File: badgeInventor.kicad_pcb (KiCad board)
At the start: 2 copper layers, 89.2 x 86 mm, 35 parts, among them P1 AUTO-PROGRAM JUMPER, P2 CONN_01X10, P22 CONN_01X10, P23 CONN_01X10, P3 LiPo, P5 OLED_I2C, P6 USB Serial, SW1 RESET, U1 SPX1117, U2 MCP73831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

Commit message: PCB v0.01
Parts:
- added SW2: SW_PUSH, open-project:SW_PUSH_SMD, F.Cu at (124.5, 146.3)
- P3: moved to B.Cu
- moved C1 59.5 mm to (115.8, 148.2), turned to 180 degrees
- moved P3 40.7 mm to (141.2, 113.5), turned to 180 degrees
- moved D5 38.7 mm to (122.7, 108.0), turned to 90 degrees
- moved D2 36.4 mm to (127.8, 108.0), turned to 270 degrees
- moved R9 30.7 mm to (149.1, 119.4)
- moved R1 29.2 mm to (164.1, 148.1), turned to 180 degrees
- moved R11 29.1 mm to (137.8, 123.4), turned to 270 degrees
- moved C5 25.0 mm to (143.3, 108.0), turned to 90 degrees
- moved D4 20.8 mm to (122.7, 137.9), turned to 90 degrees
- moved P6 20.1 mm to (132.3, 101.3)
- moved U2 20.0 mm to (149.6, 112.3)
- moved P1 18.8 mm to (119.1, 118.4), turned to 270 degrees
- moved R4 18.6 mm to (148.6, 106.9), turned to 270 degrees
- moved R10 17.7 mm to (126.2, 136.4)
- moved R3 15.4 mm to (124.7, 129.0), turned to 90 degrees
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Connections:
- P22 pad 2: /ESP8266/GPIO0 -> GND
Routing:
- net +3V3: track 1.24 -> 142.5 mm, vias 0 -> 2
- net GND: track 12.6 -> 115.2 mm, vias 0 -> 2
- net +BATT: track 0.00 -> 98.6 mm, vias 0 -> 2
- net /ESP8266/RX: track 0.00 -> 77.6 mm
- net VCC: track 11.3 -> 80.6 mm
- net /ESP8266/DTR: track 0.00 -> 61.9 mm
- net /ESP8266/GPIO14: track 0.00 -> 60.3 mm, vias 0 -> 1
- net /ESP8266/CH_PD: track 0.00 -> 59.9 mm, vias 0 -> 2
- net /ESP8266/TX: track 0.05 -> 57.7 mm, vias 0 -> 1
- net /ESP8266/RST: track 0.66 -> 49.4 mm, vias 0 -> 2
- net /ESP8266/GPIO0: track 0.12 -> 35.4 mm
- net /ESP8266/GPIO12: track 0.00 -> 31.5 mm, vias 0 -> 1
- net /ESP8266/GPIO15: track 0.00 -> 28.9 mm, vias 0 -> 1
- net /ESP8266/GPIO2: track 0.23 -> 28.3 mm
- net /ESP8266/GPIO4/SDA: track 18.3 -> 41.3 mm, vias 0 -> 1
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- added copper zone on B.Cu, net GND
- added copper zone on F.Cu, net GND
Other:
- board outline removed
- net class Vcc added: clearance 0.2, trace_width 0.31, via_dia 0.6, via_drill 0.4

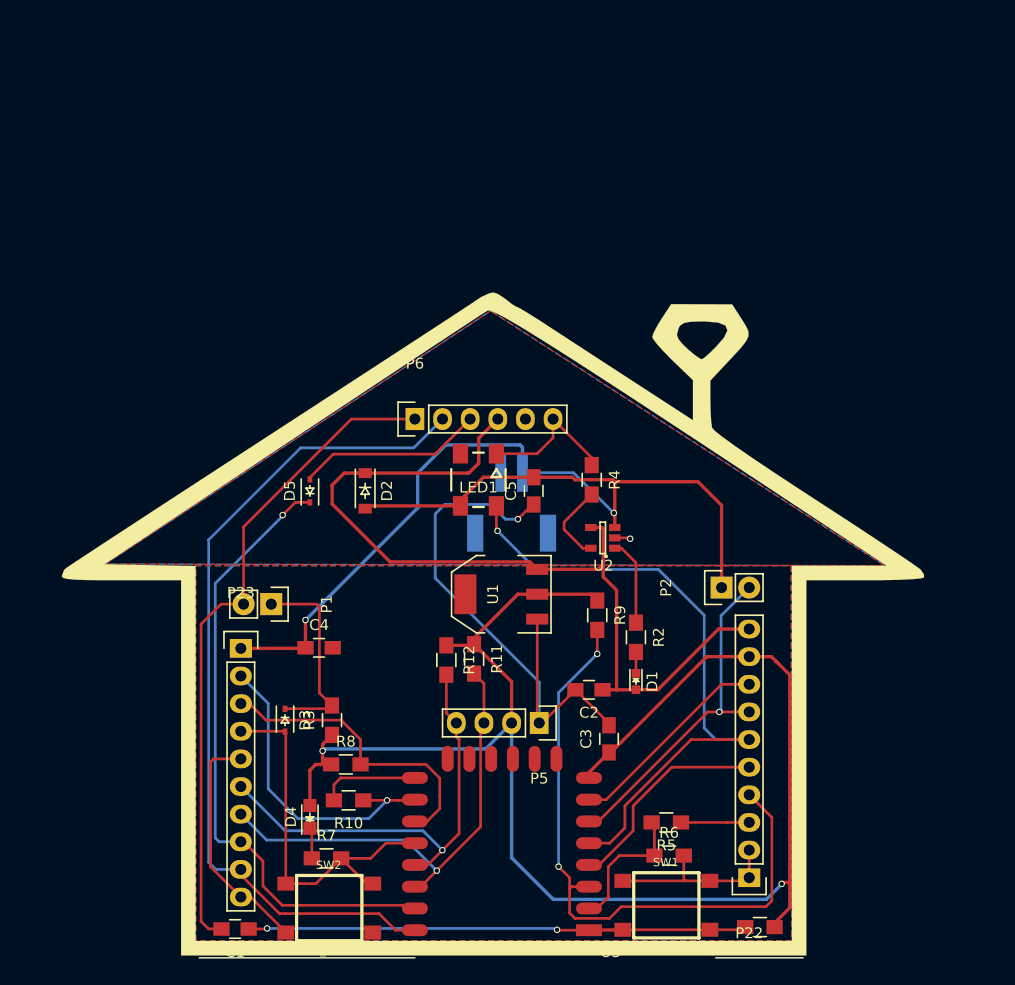
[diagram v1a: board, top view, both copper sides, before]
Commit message: Agregado EdgeCut, reacomodo de etiquetas y nombre de Serial
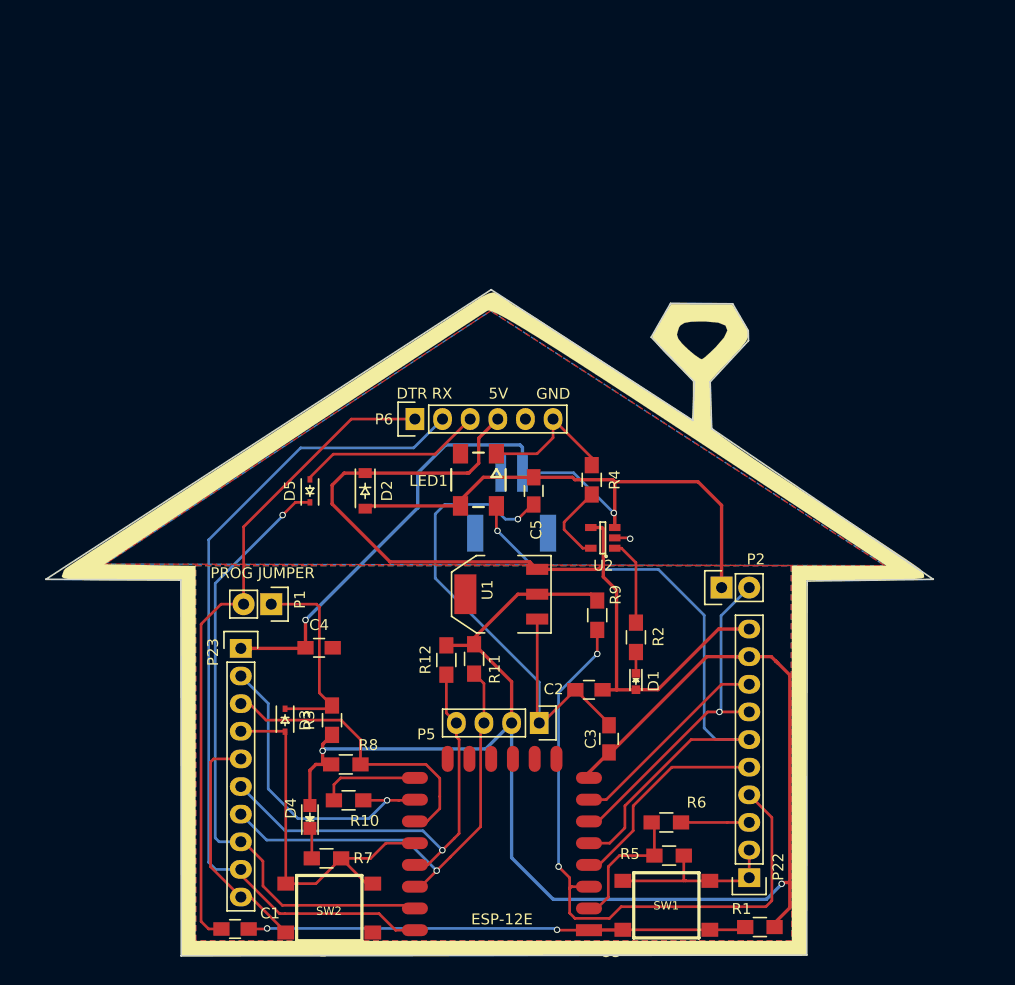
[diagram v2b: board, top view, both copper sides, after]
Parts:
- LED1: value MADW__WS2812B -> WS2812B
- P1: value AUTO-PROGRAM JUMPER -> PROG JUMPER
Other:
- board outline added: 81.6 x 61.3 mm
- board text added: "5V"
- board text added: "DTR"
- board text added: "GND"
- board text added: "RX"
